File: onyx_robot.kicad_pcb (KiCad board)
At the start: 2 copper layers, 50 x 50 mm, 36 parts, among them P1 POWER, P2 INPUTS, P3 READER, P4 FTDI, Q1 Q_NMOS_GSD, Q2 Q_NMOS_GSD, SW1 RESET, U1 ADP2301, U2 RELAY_SPDT, U3 ESP-12E

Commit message: Finished version 2
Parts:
- added D10: TVS, Diodes_SMD:SOD-523, F.Cu at (82.6, 53.5)
- added D11: TVS, Diodes_SMD:SOD-523, F.Cu at (76.9, 53.5)
- added D12: TVS, Diodes_SMD:SOD-523, F.Cu at (85.1, 56.5)
- added D3: TVS, Diodes_SMD:SOD-523, F.Cu at (86.1, 68.3)
- added D4: TVS, Diodes_SMD:SOD-523, F.Cu at (79.9, 53.5)
- added D5: TVS, Diodes_SMD:SOD-523, F.Cu at (78.4, 53.5)
- added D6: TVS, Diodes_SMD:SMA_Standard, F.Cu at (82.4, 80.3)
- added D7: TVS, Diodes_SMD:SOD-523, B.Cu at (52.0, 86.7)
- added D8: TVS, Diodes_SMD:SOD-523, B.Cu at (52.0, 76.5)
- added D9: TVS, Diodes_SMD:SOD-523, B.Cu at (52.0, 66.4)
- moved R5 2.91 mm to (74.5, 52.7)
- moved C2 2.57 mm to (84.1, 68.2)
- moved C1 2.57 mm to (82.6, 77.2)
- moved D1 2.52 mm to (82.6, 73.9)
- moved R1 2.52 mm to (72.8, 77.0)
- moved R2 2.52 mm to (72.8, 74.2)
- moved R4 2.52 mm to (76.1, 77.9)
- moved U1 2.52 mm to (76.5, 75.5)
- moved C3 2.52 mm to (76.5, 72.7)
- moved L1 2.52 mm to (78.5, 68.2)
- moved R3 2.52 mm to (78.8, 77.9)
- moved D2 1.63 mm to (71.7, 68.7)
- moved P4 1.31 mm to (71.9, 62.6)
- moved Q1 1.00 mm to (72.6, 58.8)
- turned R10 to 270 degrees
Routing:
- net GND: track 273.6 -> 291.2 mm, vias 14 -> 12
- net SCL: track 47.0 -> 52.5 mm
- net +3V3: track 92.0 -> 87.2 mm
- net SDA: track 45.7 -> 50.3 mm
- net Net-(D11-Pad1): track 17.4 -> 21.6 mm
- net PIEZO: track 21.1 -> 25.1 mm
- net DOOR: track 30.8 -> 34.7 mm
- net SNIB: track 58.3 -> 62.3 mm
- net EXIT: track 33.1 -> 37.0 mm
- net PN532_RESET: track 38.5 -> 41.2 mm, vias 1 -> 2
- net +12V: track 70.2 -> 71.9 mm
- net RELAY: track 25.6 -> 26.9 mm
- net TX: track 42.7 -> 41.5 mm
- net RX: track 43.7 -> 42.5 mm
- net ADC: track 30.8 -> 31.7 mm
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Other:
- outline, holes or cut-outs redrawn

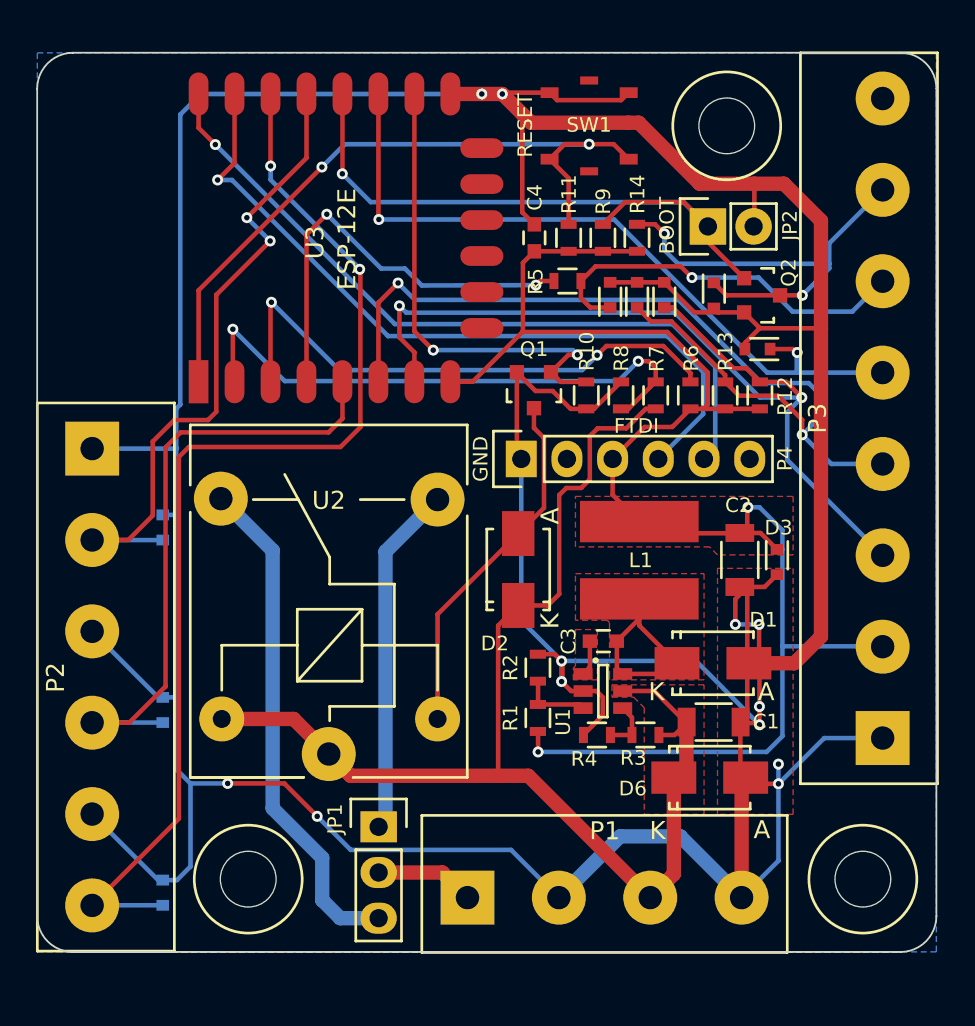
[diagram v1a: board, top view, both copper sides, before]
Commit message: Revision 3
Off-the-shelf power supply module
5V supplied to NFC reader
Piezo improved
ESD protection removed to complexity
NC contact removed from relay
VCC removed from FTDI connector
Flyback diode added to relay output
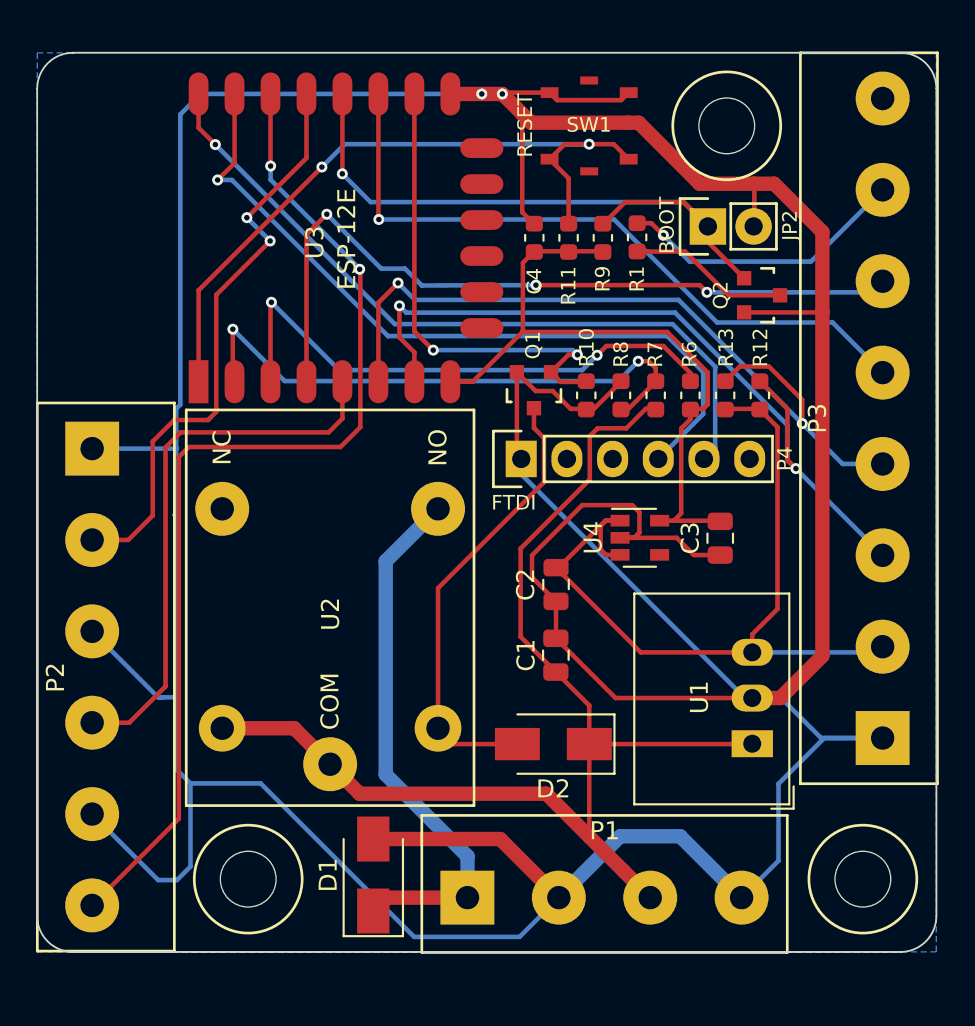
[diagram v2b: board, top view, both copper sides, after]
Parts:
- removed D10, D11, D12, D3, D4, D5, D7, D8, D9: TVS, Diodes_SMD:SOD-523
- removed D6: TVS, Diodes_SMD:SMA_Standard
- removed JP1: NO/NC, Pin_Headers:Pin_Header_Straight_1x03
- removed L1: 4.7μH 2A, timhawes:LPS6225
- removed R14: 10K, Resistors_SMD:R_0603
- removed R2, R4: 10K2 1%, Resistors_SMD:R_0603
- removed R3: 56K 1%, Resistors_SMD:R_0603
- removed R5: 100R, Resistors_SMD:R_0603
- added REF**: Hacklab_Logo_11mm, timhawes:Hacklab_Logo_11mm, B.Cu at (62.6, 55.4)
- added U4: SPX3819M5-L-3-3, Package_TO_SOT_SMD:SOT-23-5, F.Cu at (78.5, 67.0)
- C1: footprint Capacitors_SMD:C_1206 -> Capacitor_SMD:C_0805_2012Metric
- C2: value 22uF 6.3V -> 10uF 10V; footprint Capacitors_SMD:C_1206 -> Capacitor_SMD:C_0805_2012Metric
- C3: value 0.1uF 6.3V -> 10uF 6.3V; footprint Capacitors_SMD:C_0603 -> Capacitor_SMD:C_0805_2012Metric
- C4: footprint Capacitors_SMD:C_0603 -> Capacitor_SMD:C_0603_1608Metric
- D1: value B230A -> D; footprint Diodes_SMD:Diode-SMA_Standard -> Diode_SMD:D_SMA
- D2: footprint Diodes_SMD:Diode-SMA_Standard -> Diode_SMD:D_SMA
- R1: value 31K6 1% -> 1K; footprint Resistors_SMD:R_0603 -> Resistor_SMD:R_0603_1608Metric
- R10, R11, R6, R7, R8, R9: footprint Resistors_SMD:R_0603 -> Resistor_SMD:R_0603_1608Metric
- R12, R13: value 2K2 -> 4K7; footprint Resistors_SMD:R_0603 -> Resistor_SMD:R_0603_1608Metric
- U1: value ADP2301 -> R-78E5.0-1.0; footprint Housings_SOT-23_SOT-143_TSOT-6:SOT-23-6 -> Converter_DCDC:Converter_DCDC_RECOM_R-78E-0.5_THT
- U2: footprint Relays_ThroughHole:Relay_SANYOU_SRD_Series_Form_C -> timhawes:JS_RELAY
- moved R1 27.3 mm to (78.4, 50.3), turned to 270 degrees
- moved D1 22.3 mm to (63.7, 85.7), turned to 90 degrees
- moved C2 10.3 mm to (73.8, 69.6)
- moved D2 9.90 mm to (73.7, 78.4), turned to 180 degrees
- moved C1 9.53 mm to (73.8, 73.5), turned to 90 degrees
- moved U1 8.81 mm to (84.8, 78.4), turned to 90 degrees
- moved C3 8.66 mm to (83.0, 67.0), turned to 270 degrees
- moved U2 8.13 mm to (61.3, 70.9)
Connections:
- C2 pad 1: +3V3 -> +5V
- C3 pad 1: Net-(C3-Pad1) -> +3V3
- C3 pad 2: Net-(C3-Pad2) -> GND
- D1 pad 1: Net-(C3-Pad2) -> 12V_OUT
- P3 pad 2: +3V3 -> +5V
- P3 pad 6: Net-(D11-Pad1) -> LED
- P3 pad 8: (no net) -> Net-(P3-Pad8)
- P4 pad 2: (no net) -> Net-(P4-Pad2)
- P4 pad 3: +3V3 -> Net-(P4-Pad3)
- P4 pad 6: (no net) -> Net-(P4-Pad6)
- Q2 pad 3: PIEZO -> Net-(Q2-Pad3)
- R1 pad 1: +3V3 -> PIEZO
- R1 pad 2: Net-(R1-Pad2) -> Net-(Q2-Pad3)
- R12 pad 1: +3V3 -> +5V
- R13 pad 1: +3V3 -> +5V
- U1 pad 1: Net-(C3-Pad1) -> +12V
- U1 pad 3: Net-(R1-Pad2) -> +5V
- U2 pad 3: Net-(JP1-Pad1) -> 12V_OUT
- U3 pad 10: (no net) -> Net-(U3-Pad10)
- U3 pad 11: (no net) -> Net-(U3-Pad11)
- U3 pad 12: (no net) -> Net-(U3-Pad12)
- U3 pad 13: (no net) -> Net-(U3-Pad13)
- U3 pad 14: (no net) -> Net-(U3-Pad14)
- U3 pad 9: (no net) -> Net-(U3-Pad9)
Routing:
- net +3V3: track 87.2 -> 37.8 mm, vias 2 -> 0
- net +5V: track 0.00 -> 45.0 mm
- net Net-(U2-Pad4): track 28.2 -> 0.00 mm
- net 12V_OUT: track 5.52 -> 30.3 mm
- net Net-(D11-Pad1): track 21.6 -> 0.00 mm, vias 1 -> 0
- net Net-(JP1-Pad1): track 19.6 -> 0.00 mm
- net LED: track 24.2 -> 42.8 mm, vias 2 -> 3
- net Net-(C3-Pad2): track 12.5 -> 0.00 mm
- net Net-(Q2-Pad3): track 0.00 -> 8.96 mm
- net PIEZO: track 25.1 -> 16.2 mm, vias 2 -> 1
- net SCL: track 52.5 -> 43.8 mm
- net SDA: track 50.3 -> 44.0 mm
- net +12V: track 71.9 -> 66.5 mm
- net Net-(D2-Pad2): track 20.0 -> 25.2 mm
- net DOOR: track 34.7 -> 30.8 mm
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- removed copper zone on F.Cu, net +12V
- removed copper zone on F.Cu, net +3V3
- removed copper zone on F.Cu, net GND
- removed copper zone on F.Cu, net Net-(C3-Pad1)
- removed copper zone on F.Cu, net Net-(C3-Pad2)
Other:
- board text added: "5V"
- board text added: "timhawes.com/pcb/or/3 edinburghhacklab.com"
- board text removed: "3.3V"
- board text removed: "timhawes.com/or2 edinburghhacklab.com"

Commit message: Changes to text
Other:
- board text added: "RST"
- board text added: "timhawes.com/pcb/or3 edinburghhacklab.com"
- board text removed: "RESET"
- board text removed: "timhawes.com/pcb/or/3 edinburghhacklab.com"
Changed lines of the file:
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@@
     (effects (font (size 0.8128 0.8128) (thickness 0.15)))
   )
-  (gr_text RESET (at 90.17 58.42 45) (layer B.SilkS)
+  (gr_text RST (at 90.17 58.42 45) (layer B.SilkS)
     (effects (font (size 1.5 1.5) (thickness 0.3)) (justify left mirror))
   )
@@
     (effects (font (size 1.5 1.5) (thickness 0.3)) (justify left mirror))
   )
-  (gr_text "timhawes.com/pcb/or/3\nedinburghhacklab.com" (at 79.756 44.958) (layer B.SilkS)
+  (gr_text "timhawes.com/pcb/or3\nedinburghhacklab.com" (at 79.756 44.958) (layer B.SilkS)
     (effects (font (size 1.5 1.5) (thickness 0.3)) (justify left mirror))
   )

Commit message: Revision 4
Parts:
- removed R1: 1K, Resistor_SMD:R_0603_1608Metric
- added JP1: NO/NC, Connector_PinHeader_2.54mm:PinHeader_1x03_P2.54mm_Vertical, F.Cu at (64.4, 83.5)
- added R14: 10K, Resistor_SMD:R_0603_1608Metric, F.Cu at (86.0, 67.0)
- JP2: footprint Pin_Headers:Pin_Header_Straight_1x02 -> Connector_PinHeader_2.54mm:PinHeader_1x02_P2.54mm_Vertical
- moved D1 14.1 mm to (75.7, 78.3)
- moved C1 2.56 mm to (73.8, 70.9)
- moved C2 2.16 mm to (73.8, 67.4)
- moved D2 1.98 mm to (71.7, 78.3), turned to 90 degrees
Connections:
- Q2 pad 3: Net-(Q2-Pad3) -> PIEZO
- U2 pad 3: 12V_OUT -> Net-(JP1-Pad1)
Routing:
- net GND: track 288.1 -> 253.6 mm
- net Net-(JP1-Pad3): track 0.00 -> 28.4 mm
- net Net-(JP1-Pad1): track 0.00 -> 19.4 mm
- net 12V_OUT: track 30.3 -> 15.0 mm
- net PIEZO: track 16.2 -> 27.0 mm
- net Net-(Q2-Pad3): track 8.96 -> 0.00 mm
- net +5V: track 45.0 -> 47.3 mm
- net SDA: track 44.0 -> 43.0 mm
- net +12V: track 66.5 -> 65.6 mm
- net SCL: track 43.8 -> 44.5 mm
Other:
- board text added: "timhawes.com/pcb/or4 edinburghhacklab.com"
- board text removed: "timhawes.com/pcb/or3 edinburghhacklab.com"

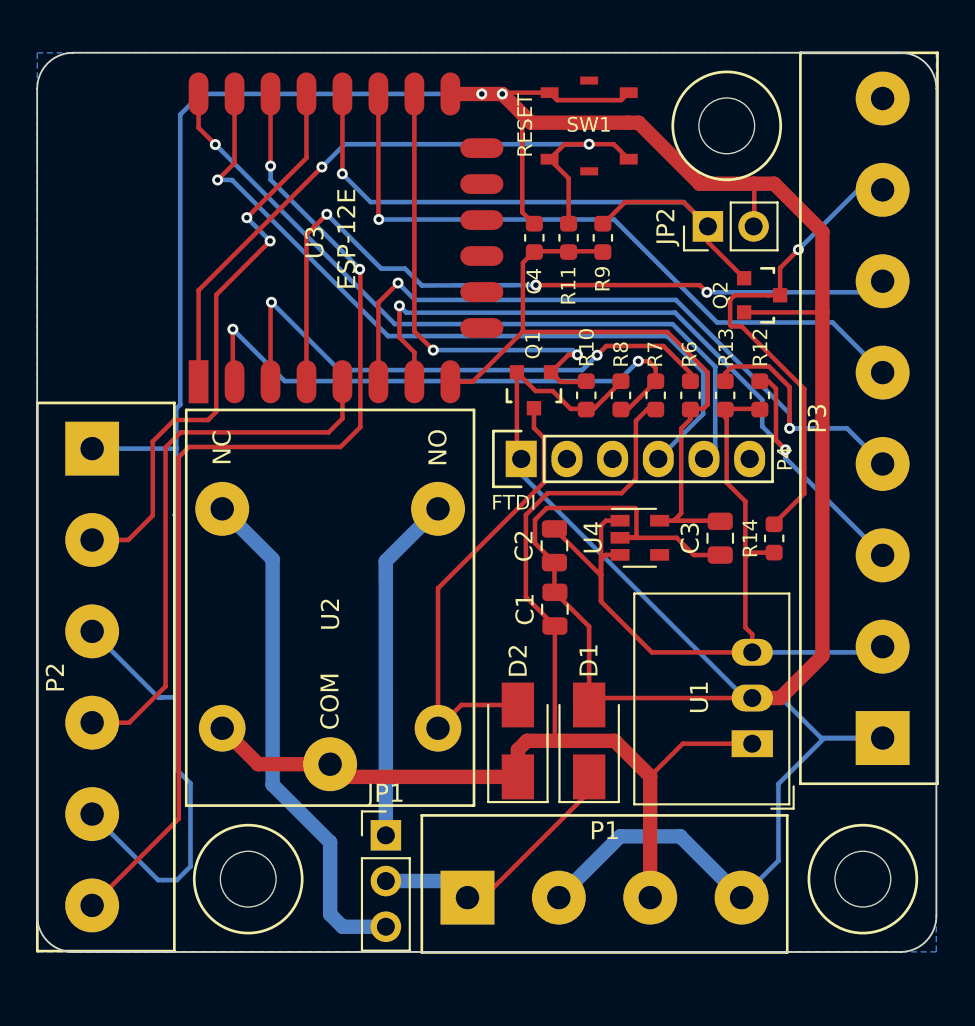
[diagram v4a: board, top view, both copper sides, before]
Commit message: No volt relay option
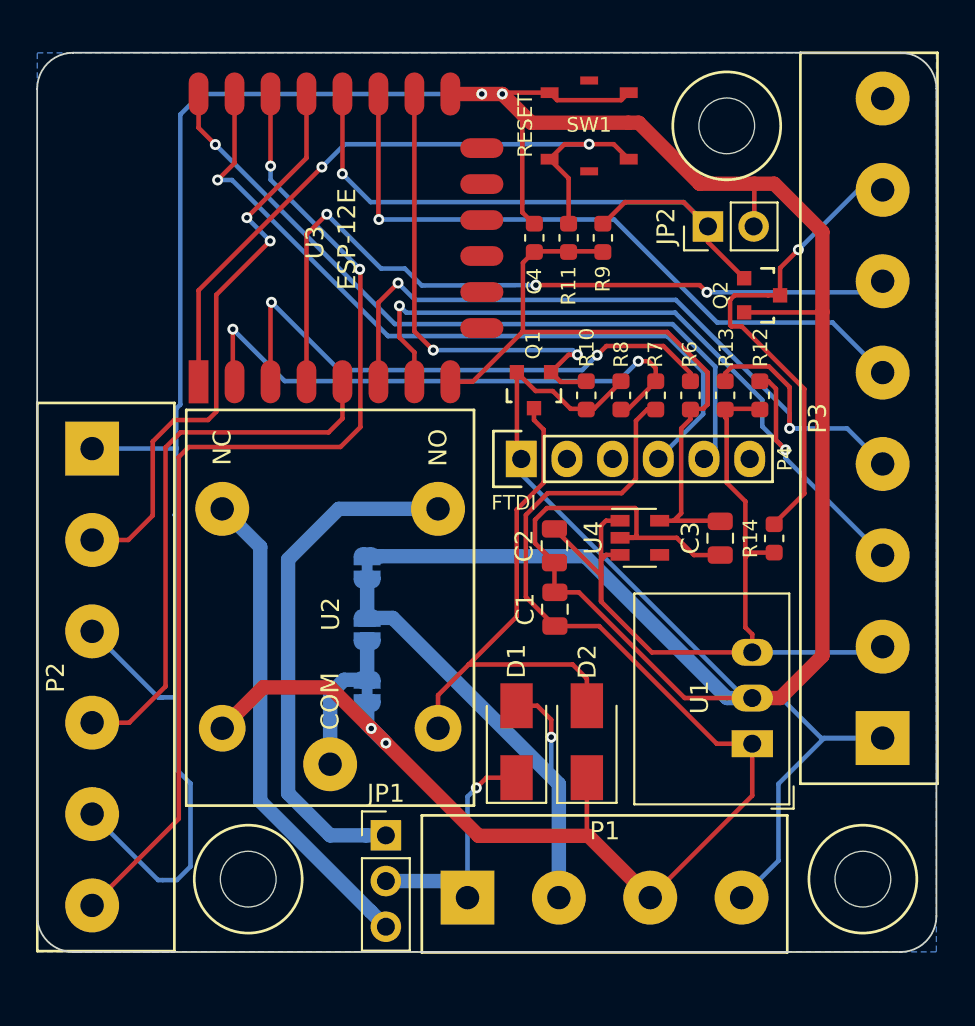
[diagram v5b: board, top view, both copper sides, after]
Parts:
- added JP3: SolderJumper_2_Bridged, Jumper:SolderJumper-2_P1.3mm_Bridged_RoundedPad1.0x1.5mm, B.Cu at (63.3, 68.6)
- added JP4: SolderJumper_2_Open, Jumper:SolderJumper-2_P1.3mm_Open_RoundedPad1.0x1.5mm, B.Cu at (63.3, 72.1)
- added JP5: SolderJumper_2_Bridged, Jumper:SolderJumper-2_P1.3mm_Bridged_RoundedPad1.0x1.5mm, B.Cu at (63.3, 75.5)
- moved D1 4.04 mm to (71.7, 78.3)
- moved D2 3.84 mm to (75.6, 78.3)
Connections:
- net 12V_OUT renamed RELAY_OUT
- D1 pad 2: GND -> RELAY_GND
- P1 pad 2: GND -> RELAY_GND
- U2 pad 1: +12V -> RELAY_IN
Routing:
- net RELAY_GND: track 0.00 -> 28.9 mm, vias 0 -> 1
- net +12V: track 65.6 -> 83.4 mm, vias 0 -> 2
- net Net-(JP1-Pad1): track 19.4 -> 28.9 mm
- net GND: track 253.6 -> 262.4 mm
- net RELAY_IN: track 0.00 -> 8.44 mm
- net Net-(D2-Pad2): track 25.4 -> 28.9 mm
- net Net-(JP1-Pad3): track 28.4 -> 27.0 mm
- net RELAY_OUT: track 15.0 -> 13.7 mm, vias 0 -> 1
